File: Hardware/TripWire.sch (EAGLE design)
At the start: 39 parts, among them X1 2X5_1.27MM

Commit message: Routing 1st draft.
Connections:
- new net N$14: D5.C, R13.2, R14.2, SV1.6
- new net N$6: D7.C, R19.2, R20.2, SV1.2
- net PIN7: no longer D5.C, R13.2, R14.2, SV1.6
- net PIN9: no longer D7.C, R19.2, R20.2, SV1.2
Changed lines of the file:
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@@
 </segment>
 <segment>
-<wire x1="15.24" y1="91.44" x2="25.4" y2="91.44" width="0.1524" layer="91"/>
+<wire x1="15.24" y1="91.44" x2="27.94" y2="91.44" width="0.1524" layer="91"/>
 <label x="15.24" y="91.44" size="1.778" layer="95"/>
+<wire x1="27.94" y1="91.44" x2="30.48" y2="93.98" width="0.1524" layer="91"/>
 </segment>
 <segment>
@@
 </segment>
 <segment>
+<pinref part="SV1" gate="1" pin="5"/>
 <pinref part="GND6" gate="1" pin="GND"/>
-<pinref part="SV1" gate="1" pin="5"/>
 <wire x1="96.52" y1="48.26" x2="99.06" y2="48.26" width="0.1524" layer="91"/>
 <wire x1="99.06" y1="48.26" x2="99.06" y2="45.72" width="0.1524" layer="91"/>
+<pinref part="SV1" gate="1" pin="1"/>
+<wire x1="99.06" y1="45.72" x2="99.06" y2="43.18" width="0.1524" layer="91"/>
+<wire x1="99.06" y1="43.18" x2="96.52" y2="43.18" width="0.1524" layer="91"/>
 <pinref part="SV1" gate="1" pin="3"/>
-<wire x1="99.06" y1="45.72" x2="99.06" y2="43.18" width="0.1524" layer="91"/>
 <wire x1="96.52" y1="45.72" x2="99.06" y2="45.72" width="0.1524" layer="91"/>
-<pinref part="SV1" gate="1" pin="1"/>
-<wire x1="96.52" y1="43.18" x2="99.06" y2="43.18" width="0.1524" layer="91"/>
+<junction x="99.06" y="48.26"/>
+<junction x="99.06" y="45.72"/>
+<junction x="99.06" y="43.18"/>
 </segment>
 </net>
@@
 </segment>
 <segment>
-<wire x1="83.82" y1="48.26" x2="81.28" y2="48.26" width="0.1524" layer="91"/>
-<pinref part="SV1" gate="1" pin="6"/>
-<wire x1="81.28" y1="48.26" x2="81.28" y2="63.5" width="0.1524" layer="91"/>
-<pinref part="R13" gate="G$1" pin="2"/>
-<pinref part="R14" gate="G$1" pin="2"/>
-<wire x1="43.18" y1="63.5" x2="53.34" y2="63.5" width="0.1524" layer="91"/>
-<pinref part="D5" gate="G$1" pin="C"/>
-<wire x1="53.34" y1="63.5" x2="81.28" y2="63.5" width="0.1524" layer="91"/>
-<wire x1="53.34" y1="66.04" x2="53.34" y2="63.5" width="0.1524" layer="91"/>
-</segment>
-<segment>
 <pinref part="R14" gate="G$1" pin="1"/>
 <wire x1="33.02" y1="63.5" x2="25.4" y2="63.5" width="0.1524" layer="91"/>
@@
 </segment>
 <segment>
-<wire x1="83.82" y1="43.18" x2="81.28" y2="43.18" width="0.1524" layer="91"/>
-<pinref part="SV1" gate="1" pin="2"/>
-<wire x1="81.28" y1="12.7" x2="81.28" y2="43.18" width="0.1524" layer="91"/>
-<pinref part="D7" gate="G$1" pin="C"/>
-<wire x1="81.28" y1="12.7" x2="53.34" y2="12.7" width="0.1524" layer="91"/>
-<wire x1="53.34" y1="12.7" x2="53.34" y2="15.24" width="0.1524" layer="91"/>
-<pinref part="R19" gate="G$1" pin="2"/>
-<pinref part="R20" gate="G$1" pin="2"/>
-<wire x1="43.18" y1="12.7" x2="53.34" y2="12.7" width="0.1524" layer="91"/>
-</segment>
-<segment>
 <pinref part="R20" gate="G$1" pin="1"/>
 <wire x1="33.02" y1="12.7" x2="25.4" y2="12.7" width="0.1524" layer="91"/>
@@
 <pinref part="D5" gate="G$1" pin="A"/>
 <wire x1="53.34" y1="78.74" x2="53.34" y2="73.66" width="0.1524" layer="91"/>
+<junction x="53.34" y="78.74"/>
 </segment>
 </net>
@@
 <wire x1="53.34" y1="38.1" x2="53.34" y2="40.64" width="0.1524" layer="91"/>
 <wire x1="43.18" y1="38.1" x2="53.34" y2="38.1" width="0.1524" layer="91"/>
+<junction x="53.34" y="38.1"/>
+<junction x="43.18" y="38.1"/>
 </segment>
 </net>
@@
 <pinref part="R18" gate="G$1" pin="1"/>
 <wire x1="53.34" y1="48.26" x2="53.34" y2="53.34" width="0.1524" layer="91"/>
+<junction x="53.34" y="53.34"/>
 </segment>
 </net>
@@
 <pinref part="R21" gate="G$1" pin="2"/>
 <wire x1="53.34" y1="22.86" x2="53.34" y2="27.94" width="0.1524" layer="91"/>
+<junction x="53.34" y="27.94"/>
 </segment>
 </net>
@@
 <pinref part="D1" gate="G$1" pin="A"/>
 <wire x1="119.38" y1="124.46" x2="119.38" y2="119.38" width="0.1524" layer="91"/>
+<junction x="119.38" y="124.46"/>
 </segment>
 </net>
@@
 <pinref part="R2" gate="G$1" pin="2"/>
 <wire x1="119.38" y1="109.22" x2="111.76" y2="109.22" width="0.1524" layer="91"/>
+<junction x="119.38" y="109.22"/>
+<junction x="111.76" y="109.22"/>
 </segment>
 </net>
@@
 <wire x1="119.38" y1="81.28" x2="119.38" y2="78.74" width="0.1524" layer="91"/>
 <wire x1="111.76" y1="78.74" x2="119.38" y2="78.74" width="0.1524" layer="91"/>
+<junction x="119.38" y="78.74"/>
+<junction x="111.76" y="78.74"/>
 </segment>
 </net>
@@
 <pinref part="D2" gate="G$1" pin="A"/>
 <wire x1="119.38" y1="93.98" x2="119.38" y2="88.9" width="0.1524" layer="91"/>
+<junction x="119.38" y="93.98"/>
 </segment>
 </net>
@@
 <wire x1="165.1" y1="111.76" x2="165.1" y2="109.22" width="0.1524" layer="91"/>
 <wire x1="157.48" y1="109.22" x2="165.1" y2="109.22" width="0.1524" layer="91"/>
+<junction x="165.1" y="109.22"/>
+<junction x="157.48" y="109.22"/>
 </segment>
 </net>
@@
 <pinref part="D3" gate="G$1" pin="A"/>
 <wire x1="165.1" y1="124.46" x2="165.1" y2="119.38" width="0.1524" layer="91"/>
+<junction x="165.1" y="124.46"/>
 </segment>
 </net>
@@
 <wire x1="165.1" y1="81.28" x2="165.1" y2="78.74" width="0.1524" layer="91"/>
 <wire x1="165.1" y1="78.74" x2="157.48" y2="78.74" width="0.1524" layer="91"/>
+<junction x="165.1" y="78.74"/>
+<junction x="157.48" y="78.74"/>
 </segment>
 </net>
@@
 <pinref part="D4" gate="G$1" pin="A"/>
 <wire x1="165.1" y1="93.98" x2="165.1" y2="88.9" width="0.1524" layer="91"/>
-</segment>
-</net>
+<junction x="165.1" y="93.98"/>
+</segment>
+</net>
+<net name="N$14" class="0">
+<segment>
+<pinref part="R13" gate="G$1" pin="2"/>
+<pinref part="R14" gate="G$1" pin="2"/>
+<pinref part="SV1" gate="1" pin="6"/>
+<wire x1="43.18" y1="63.5" x2="53.34" y2="63.5" width="0.1524" layer="91"/>
+<wire x1="53.34" y1="63.5" x2="81.28" y2="63.5" width="0.1524" layer="91"/>
+<wire x1="81.28" y1="63.5" x2="81.28" y2="48.26" width="0.1524" layer="91"/>
+<pinref part="D5" gate="G$1" pin="C"/>
+<wire x1="53.34" y1="66.04" x2="53.34" y2="63.5" width="0.1524" layer="91"/>
+<junction x="53.34" y="63.5"/>
+<junction x="43.18" y="63.5"/>
+</segment>
+</net>
+<net name="N$6" class="0">
+<segment>
+<pinref part="R19" gate="G$1" pin="2"/>
+<pinref part="R20" gate="G$1" pin="2"/>
+<pinref part="SV1" gate="1" pin="2"/>
+<wire x1="43.18" y1="12.7" x2="53.34" y2="12.7" width="0.1524" layer="91"/>
+<wire x1="53.34" y1="12.7" x2="81.28" y2="12.7" width="0.1524" layer="91"/>
+<wire x1="81.28" y1="12.7" x2="81.28" y2="43.18" width="0.1524" layer="91"/>
+<pinref part="D7" gate="G$1" pin="C"/>
+<wire x1="53.34" y1="15.24" x2="53.34" y2="12.7" width="0.1524" layer="91"/>
+<junction x="53.34" y="12.7"/>
+<junction x="43.18" y="12.7"/>
+</segment>
+</net>

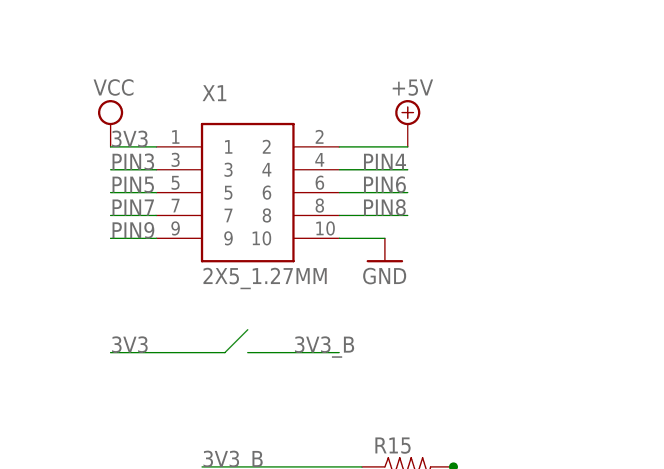
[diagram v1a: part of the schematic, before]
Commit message: All DRC checks passed.
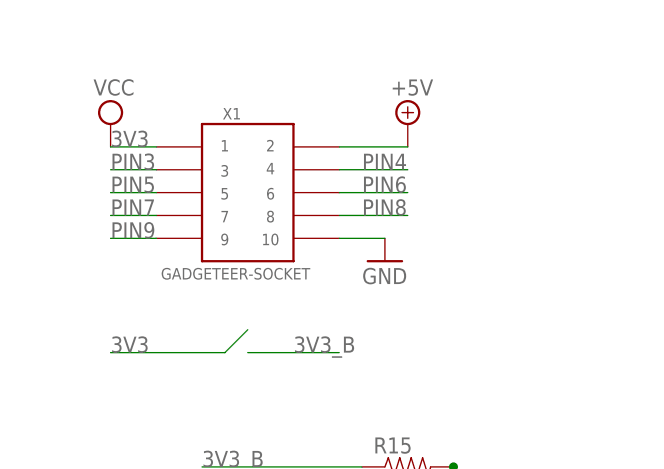
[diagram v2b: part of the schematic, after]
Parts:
- X1: value 2X5_1.27MM -> GADGETEER-SOCKET; device GHI:2X5_1.27MM -> SoftDust:GADGETEER-SOCKET
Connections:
- net +5V: now also X1.P$2; no longer X1.2
- net 3V3: now also X1.P$1; no longer X1.1
- net GND: now also X1.P$10; no longer X1.10
- net PIN3: now also X1.P$3; no longer X1.3
- net PIN4: now also X1.P$4; no longer X1.4
- net PIN5: now also X1.P$5; no longer X1.5
- net PIN6: now also X1.P$6; no longer X1.6
- net PIN7: now also X1.P$7; no longer X1.7
- net PIN8: now also X1.P$8; no longer X1.8
- net PIN9: now also X1.P$9; no longer X1.9
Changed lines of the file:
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@@
 <part name="V1" library="supply2" deviceset="+5V" device=""/>
 <part name="V2" library="supply2" deviceset="VCC" device=""/>
-<part name="X1" library="GHI" deviceset="2X5_1.27MM" device=""/>
+<part name="X1" library="SoftDust" deviceset="GADGETEER-SOCKET" device=""/>
 <part name="LOGO1" library="Logo" deviceset="LOGO-OSHW-FILL" device="X0200-NT"/>
 <part name="U$1" library="SoftDust" deviceset="SPADE-TERMINAL" device="PTH"/>
@@
 <instance part="V1" gate="+5V" x="48.26" y="116.84"/>
 <instance part="V2" gate="G$1" x="15.24" y="116.84"/>
-<instance part="X1" gate="G$1" x="30.48" y="109.22"/>
+<instance part="X1" gate="G$1" x="30.48" y="109.22" smashed="yes">
+<attribute name="NAME" x="27.686" y="117.348" size="1.27" layer="95"/>
+<attribute name="VALUE" x="20.828" y="99.568" size="1.27" layer="96"/>
+</instance>
 <instance part="LOGO1" gate="G$1" x="10.16" y="7.62"/>
 <instance part="U$1" gate="G$1" x="119.38" y="109.22"/>
@@
 <wire x1="15.24" y1="114.3" x2="20.32" y2="114.3" width="0.1524" layer="91"/>
 <pinref part="V2" gate="G$1" pin="VCC"/>
-<pinref part="X1" gate="G$1" pin="1"/>
+<pinref part="X1" gate="G$1" pin="P$1"/>
 <label x="15.24" y="114.3" size="1.778" layer="95"/>
 </segment>
@@
 <wire x1="45.72" y1="104.14" x2="40.64" y2="104.14" width="0.1524" layer="91"/>
 <pinref part="GND1" gate="1" pin="GND"/>
-<pinref part="X1" gate="G$1" pin="10"/>
+<pinref part="X1" gate="G$1" pin="P$10"/>
 </segment>
 <segment>
@@
 <wire x1="48.26" y1="114.3" x2="40.64" y2="114.3" width="0.1524" layer="91"/>
 <pinref part="V1" gate="+5V" pin="+5V"/>
-<pinref part="X1" gate="G$1" pin="2"/>
+<pinref part="X1" gate="G$1" pin="P$2"/>
 </segment>
 </net>
 <net name="PIN3" class="0">
 <segment>
-<pinref part="X1" gate="G$1" pin="3"/>
+<pinref part="X1" gate="G$1" pin="P$3"/>
 <wire x1="20.32" y1="111.76" x2="15.24" y2="111.76" width="0.1524" layer="91"/>
 <label x="15.24" y="111.76" size="1.778" layer="95"/>
@@
 <net name="PIN4" class="0">
 <segment>
-<pinref part="X1" gate="G$1" pin="4"/>
+<pinref part="X1" gate="G$1" pin="P$4"/>
 <wire x1="40.64" y1="111.76" x2="48.26" y2="111.76" width="0.1524" layer="91"/>
 <label x="43.18" y="111.76" size="1.778" layer="95"/>
@@
 <net name="PIN5" class="0">
 <segment>
-<pinref part="X1" gate="G$1" pin="5"/>
+<pinref part="X1" gate="G$1" pin="P$5"/>
 <wire x1="20.32" y1="109.22" x2="15.24" y2="109.22" width="0.1524" layer="91"/>
 <label x="15.24" y="109.22" size="1.778" layer="95"/>
@@
 <net name="PIN7" class="0">
 <segment>
-<pinref part="X1" gate="G$1" pin="7"/>
+<pinref part="X1" gate="G$1" pin="P$7"/>
 <wire x1="20.32" y1="106.68" x2="15.24" y2="106.68" width="0.1524" layer="91"/>
 <label x="15.24" y="106.68" size="1.778" layer="95"/>
@@
 <net name="PIN9" class="0">
 <segment>
-<pinref part="X1" gate="G$1" pin="9"/>
+<pinref part="X1" gate="G$1" pin="P$9"/>
 <wire x1="20.32" y1="104.14" x2="15.24" y2="104.14" width="0.1524" layer="91"/>
 <label x="15.24" y="104.14" size="1.778" layer="95"/>
@@
 <net name="PIN6" class="0">
 <segment>
-<pinref part="X1" gate="G$1" pin="6"/>
+<pinref part="X1" gate="G$1" pin="P$6"/>
 <wire x1="40.64" y1="109.22" x2="48.26" y2="109.22" width="0.1524" layer="91"/>
 <label x="43.18" y="109.22" size="1.778" layer="95"/>
@@
 <net name="PIN8" class="0">
 <segment>
-<pinref part="X1" gate="G$1" pin="8"/>
+<pinref part="X1" gate="G$1" pin="P$8"/>
 <wire x1="40.64" y1="106.68" x2="48.26" y2="106.68" width="0.1524" layer="91"/>
 <label x="43.18" y="106.68" size="1.778" layer="95"/>

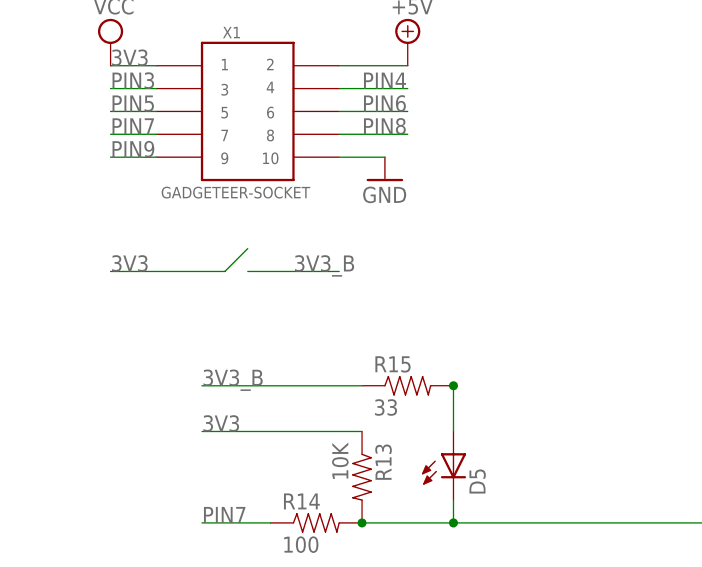
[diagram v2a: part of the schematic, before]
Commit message: Added LED enable junction pads.
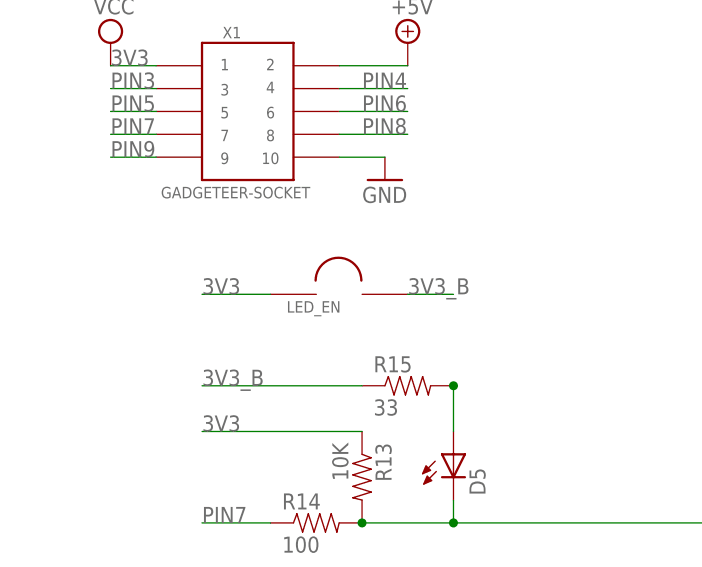
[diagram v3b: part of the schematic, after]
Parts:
- added LED_EN: SOLDER-JUNCTION, SoftDust:SOLDER-JUNCTION
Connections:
- net 3V3: now also LED_EN.P$1
- net 3V3_B: now also LED_EN.P$2
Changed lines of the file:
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@@
 <part name="R20" library="SparkFun-Resistors" deviceset="RESISTOR" device="0603-RES" value="100"/>
 <part name="R21" library="SparkFun-Resistors" deviceset="RESISTOR" device="0603-RES" value="33"/>
+<part name="LED_EN" library="SoftDust" deviceset="SOLDER-JUNCTION" device=""/>
 </parts>
 <sheets>
@@
 <instance part="R20" gate="G$1" x="38.1" y="12.7"/>
 <instance part="R21" gate="G$1" x="48.26" y="27.94"/>
+<instance part="LED_EN" gate="G$1" x="40.64" y="88.9" smashed="yes">
+<attribute name="NAME" x="34.798" y="86.868" size="1.27" layer="95"/>
+</instance>
 </instances>
 <busses>
@@
 </segment>
 <segment>
-<wire x1="15.24" y1="91.44" x2="27.94" y2="91.44" width="0.1524" layer="91"/>
-<label x="15.24" y="91.44" size="1.778" layer="95"/>
-<wire x1="27.94" y1="91.44" x2="30.48" y2="93.98" width="0.1524" layer="91"/>
-</segment>
-<segment>
 <pinref part="R16" gate="G$1" pin="1"/>
 <wire x1="43.18" y1="48.26" x2="25.4" y2="48.26" width="0.1524" layer="91"/>
@@
 <wire x1="157.48" y1="88.9" x2="139.7" y2="88.9" width="0.1524" layer="91"/>
 <label x="139.7" y="88.9" size="1.778" layer="95"/>
+</segment>
+<segment>
+<pinref part="LED_EN" gate="G$1" pin="P$1"/>
+<wire x1="33.02" y1="88.9" x2="25.4" y2="88.9" width="0.1524" layer="91"/>
+<label x="25.4" y="88.9" size="1.778" layer="95"/>
 </segment>
 </net>
@@
 </segment>
 <segment>
-<wire x1="30.48" y1="91.44" x2="40.64" y2="91.44" width="0.1524" layer="91"/>
-<label x="35.56" y="91.44" size="1.778" layer="95"/>
-</segment>
-<segment>
 <pinref part="R18" gate="G$1" pin="2"/>
 <wire x1="43.18" y1="53.34" x2="25.4" y2="53.34" width="0.1524" layer="91"/>
@@
 <label x="139.7" y="93.98" size="1.778" layer="95"/>
 </segment>
-</net>
+<segment>
+<pinref part="LED_EN" gate="G$1" pin="P$2"/>
+<wire x1="48.26" y1="88.9" x2="53.34" y2="88.9" width="0.1524" layer="91"/>
+<label x="48.26" y="88.9" size="1.778" layer="95"/>
+</segment>
+</net>
